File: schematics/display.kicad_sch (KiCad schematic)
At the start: 56 parts, among them Q11 2N3906, Q9 2N3906, U14 74AC138, U15 74HC245, U16 74HC245, U17 74HC245, U18 74HC245, U19 74HC4511, U20 74HC4511, U25 RED, U26 RED, U27 RED, U28 RED, U29 RED, U30 RED, U31 RED, U32 RED, U33 RED

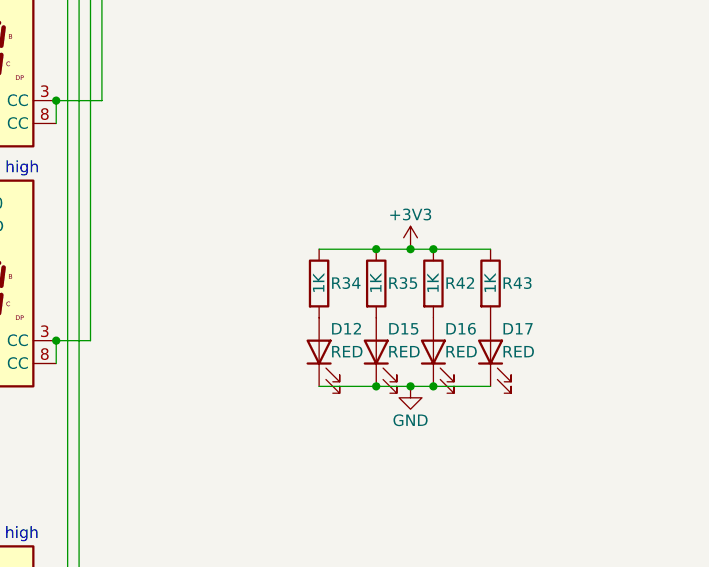
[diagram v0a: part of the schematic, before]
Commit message: increased resistor for colon LEDs
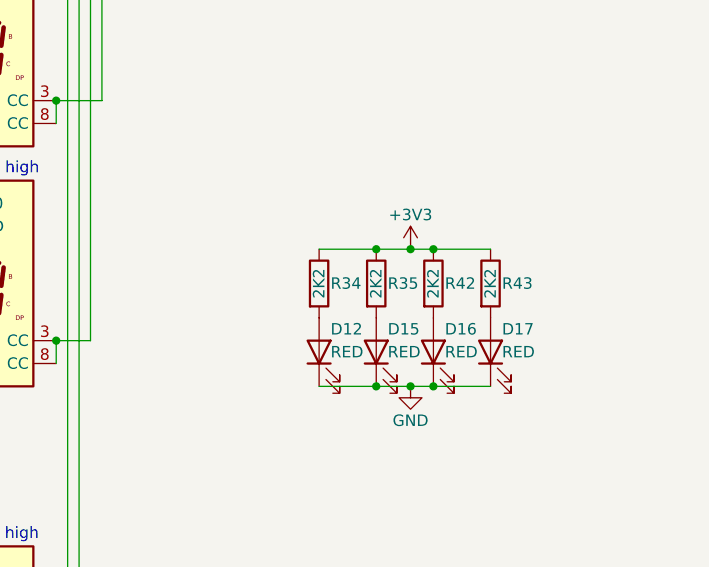
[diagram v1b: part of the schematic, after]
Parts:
- R34, R35, R42, R43: value 1K -> 2K2
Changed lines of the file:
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@@
 			)
 		)
-		(property "Value" "1K"
+		(property "Value" "2K2"
 			(at 238.76 92.71 90)
 			(show_name no)
@@
 			)
 		)
-		(property "Value" "1K"
+		(property "Value" "2K2"
 			(at 245.11 92.71 90)
 			(show_name no)
@@
 			)
 		)
-		(property "Value" "1K"
+		(property "Value" "2K2"
 			(at 226.06 92.71 90)
 			(show_name no)
@@
 			)
 		)
-		(property "Value" "1K"
+		(property "Value" "2K2"
 			(at 232.41 92.71 90)
 			(show_name no)

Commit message: started a second version
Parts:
- removed C32: 100N, Package_SO:SOIC-8_3.9x4.9mm_P1.27mm, symbol Device:C
- removed Q11, Q9: 2N3906, Package_TO_SOT_THT:TO-92_Inline, symbol Transistor_BJT:2N3906
- removed R17, R18: 4K7, symbol Device:R
- removed R19, R20, R21, R22, R23, R24, R25, R26, R27, R28, R29, R30, R31, R32, R33: 220R, symbol Device:R
- removed R57: 1K, symbol Device:R
- removed R58: 10K, symbol Device:R
- removed U15, U16, U17, U18: 74HC245, Package_SO:SOIC-16W_7.5x10.3mm_P1.27mm, symbol 74xx:74HC245
- removed U20: 74HC4511, symbol bvclock:74HC4511
- removed U25, U26, U27, U28, U29, U30, U31, U32, U33: RED, Display_7Segment:HDSP-A151, symbol Display_Character:HDSP-A153
- added Q1, Q2, Q21, Q22, Q3, Q4, Q5, Q6, Q7: 2N3904, Package_TO_SOT_THT:TO-92_Inline, symbol Transistor_BJT:2N3904
- added Q10, Q11, Q12, Q13, Q14, Q15, Q8, Q9: S9012, Package_TO_SOT_THT:TO-92_Inline, symbol Transistor_BJT:Q_PNP_EBC
- added R36, R38, R39, R40, R41, R46, R47: 10K, symbol Device:R
- added R48, R49, R51, R53, R54: 1K, symbol Device:R
- added R79: 75K, symbol Device:R
- added R81: 15K, symbol Device:R
- added U15, U21, U22, U23, U24, U25, U26, U3, U37: 5161BS, Display_7Segment:KCSC02-105, symbol Display_Character:KCSA02-105
- added U16, U17, U18, U20: 74HC251, Package_DIP:DIP-28_W15.24mm, symbol 74xx:74LS251
- R34, R35, R42, R43: value 2K2 -> 1K
- R52: value 10K -> 1K
- R55: value 680R -> 1K
- R56: value 150R -> 120R
- U14: value 74AC138 -> 74HC138
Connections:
- net ~{AMPM} is gone; now on an unnamed net: R50.2
- net +3V3: now also Q10.1 (E), Q11.1 (E), Q12.1 (E), Q13.1 (E), Q14.1 (E), Q15.1 (E), Q8.1 (E), Q9.1 (E), U16.16 (V_{CC}), U17.16 (V_{CC}), U18.16 (V_{CC}), U20.16 (V_{CC}), U37.3 (CA), U37.8 (CA); no longer R55.2, R56.2, U19.4 (~{BL}), U19.5 (~{LE})
- net CS0: now also U20.4 (I_{0})
- net CS1: now also U18.4 (I_{0})
- net CS2: now also U17.4 (I_{0})
- net CS3: now also U16.4 (I_{0})
- net DS0: now also U20.3 (I_{1})
- net DS1: now also U18.3 (I_{1})
- net DS2: now also U17.3 (I_{1})
- net DS3: now also U16.3 (I_{1})
- net GND: now also R56.1, U19.5 (~{LE}), Q1.1 (E), Q2.1 (E), Q21.1 (E), Q22.1 (E), Q3.1 (E), Q4.1 (E), Q5.1 (E), Q6.1 (E), Q7.1 (E), U16.1 (I_{3}), U16.12 (I_{7}), U16.14 (I_{5}), U16.7 (~{OE}), U16.8 (GND), U17.12 (I_{7}), U17.7 (~{OE}), U17.8 (GND), U18.7 (~{OE}), U18.8 (GND), U20.7 (~{OE}), U20.8 (GND); no longer U14.3 (A2)
- net HH0: now also U20.12 (I_{7})
- net HH1: now also U18.12 (I_{7})
- net HL0: now also U20.13 (I_{6})
- net HL1: now also U18.13 (I_{6})
- net HL2: now also U17.13 (I_{6})
- net HL3: now also U16.13 (I_{6})
- net MH0: now also U20.14 (I_{5})
- net MH1: now also U18.14 (I_{5})
- net MH2: now also U17.14 (I_{5})
- net ML0: now also U20.15 (I_{4})
- net ML1: now also U18.15 (I_{4})
- net ML2: now also U17.15 (I_{4})
- net ML3: now also U16.15 (I_{4})
- net SH0: now also U20.1 (I_{3})
- net SH1: now also U18.1 (I_{3})
- net SH2: now also U17.1 (I_{3})
- net SL0: now also U20.2 (I_{2})
- net SL1: now also U18.2 (I_{2})
- net SL2: now also U17.2 (I_{2})
- net SL3: now also U16.2 (I_{2})
- net ~{BL}: now also U19.4 (~{BL})
- net at U19.12 (b): now also R46.1
- net at R52.2: now also U14.12 (~{Y3})
- net at U19.10 (d): now also R40.1
- net at U19.6 (D_{3}): now also U16.5 (Y)
- net at U19.2 (D_{2}): now also U17.5 (Y)
- net at U19.1 (D_{1}): now also U18.5 (Y)
- net at U19.7 (D_{0}): now also U20.5 (Y)
- net at U19.13 (a): now also R47.1
- net at U19.11 (c): now also R41.1
- net at U14.14 (~{Y1}): now also R54.2
- net at U19.15 (f): now also R38.1
- net at U14.15 (~{Y0}): now also R55.2
- net at R50.1: now also Q10.2 (B)
- net at R55.1: now also Q15.2 (B)
- net at U19.9 (e): now also R39.1
- net at U14.13 (~{Y2}): now also R53.2
- net at U19.14 (g): now also R36.1
- net at U14.11 (~{Y4}): now also R51.2
- net at U14.7 (~{Y7}): now also R48.2
- net at U14.9 (~{Y6}): now also R49.2
- net S0 renamed SEL0
- net SEL0: now also U16.11 (S0), U17.11 (S0), U18.11 (S0), U20.11 (S0)
- net S1 renamed SEL1
- net SEL1: now also U16.10 (S1), U17.10 (S1), U18.10 (S1), U20.10 (S1)
- net ~{AM}: no longer names the net of R52.1
- net ~{AM}: now also Q12.2 (B)
- new net: Q22.2 (B), R81.2
- new net: Q22.3 (C), U37.1 (E), U37.10 (G), U37.5 (DP), U37.6 (B), U37.7 (A), U37.9 (F)
- new net: Q6.2 (B), R46.2
- new net: Q6.3 (C), U15.6 (B), U21.6 (B), U22.6 (B), U23.6 (B), U24.6 (B), U25.6 (B), U26.6 (B), U3.6 (B)
- new net: Q3.3 (C), U15.1 (E), U21.1 (E), U22.1 (E), U23.1 (E), U24.1 (E), U25.1 (E), U26.1 (E), U3.1 (E)
- new net: Q1.3 (C), U15.10 (G), U21.10 (G), U22.10 (G), U23.10 (G), U24.10 (G), U25.10 (G), U26.10 (G), U3.10 (G)
- new net: Q4.3 (C), U15.2 (D), U21.2 (D), U22.2 (D), U23.2 (D), U24.2 (D), U25.2 (D), U26.2 (D), U3.2 (D)
- new net: Q13.3 (C), U24.3 (CA), U24.8 (CA)
- new net: Q5.3 (C), U15.4 (C), U21.4 (C), U22.4 (C), U23.4 (C), U24.4 (C), U25.4 (C), U26.4 (C), U3.4 (C)
- new net: R56.2, U24.5 (DP)
- new net: Q7.3 (C), U15.7 (A), U21.7 (A), U22.7 (A), U23.7 (A), U24.7 (A), U25.7 (A), U26.7 (A), U3.7 (A)
- new net: Q2.3 (C), U15.9 (F), U21.9 (F), U22.9 (F), U23.9 (F), U24.9 (F), U25.9 (F), U26.9 (F), U3.9 (F)
- new net: Q15.3 (C), U26.3 (CA), U26.8 (CA)
- new net: Q4.2 (B), R40.2
- new net: Q3.2 (B), R39.2
- new net: Q7.2 (B), R47.2
- new net: Q1.2 (B), R36.2
- new net: Q8.2 (B), R48.1
- new net: Q11.3 (C), U22.3 (CA), U22.8 (CA)
- new net: Q12.3 (C), U23.3 (CA), U23.8 (CA)
- new net: Q2.2 (B), R38.2
- new net: Q11.2 (B), R51.1
- new net: Q21.2 (B), R79.2
- new net: Q10.3 (C), U21.3 (CA), U21.8 (CA)
- new net: Q13.2 (B), R53.1
- new net: Q14.2 (B), R54.1
- new net: Q14.3 (C), U25.3 (CA), U25.8 (CA)
- new net: Q9.2 (B), R49.1
- new net: Q9.3 (C), U15.3 (CA), U15.8 (CA)
- new net: Q5.2 (B), R41.2
- new net: Q21.3 (C), U37.4 (C)
- new net AM: R79.1
- new net AMPM: R81.1
- new net SEL2: U14.3 (C), U16.9 (S2), U17.9 (S2), U18.9 (S2), U20.9 (S2)
- new net ~{HHSEL}: Q8.3 (C), U3.3 (CA), U3.8 (CA)
- no-connect marks 14 -> 12
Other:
- note removed: "AM/PM"
- note removed: "centiseconds"
- note removed: "deciseconds"
- note removed: "hours high"
- note removed: "hours low"
- note removed: "minutes high"
- note removed: "minutes low"
- note removed: "seconds high"
- note removed: "seconds low"
- moved on the sheet: C26, C27, C28, C29, C30, C31, D12, D15, D16, D17, R34, R35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

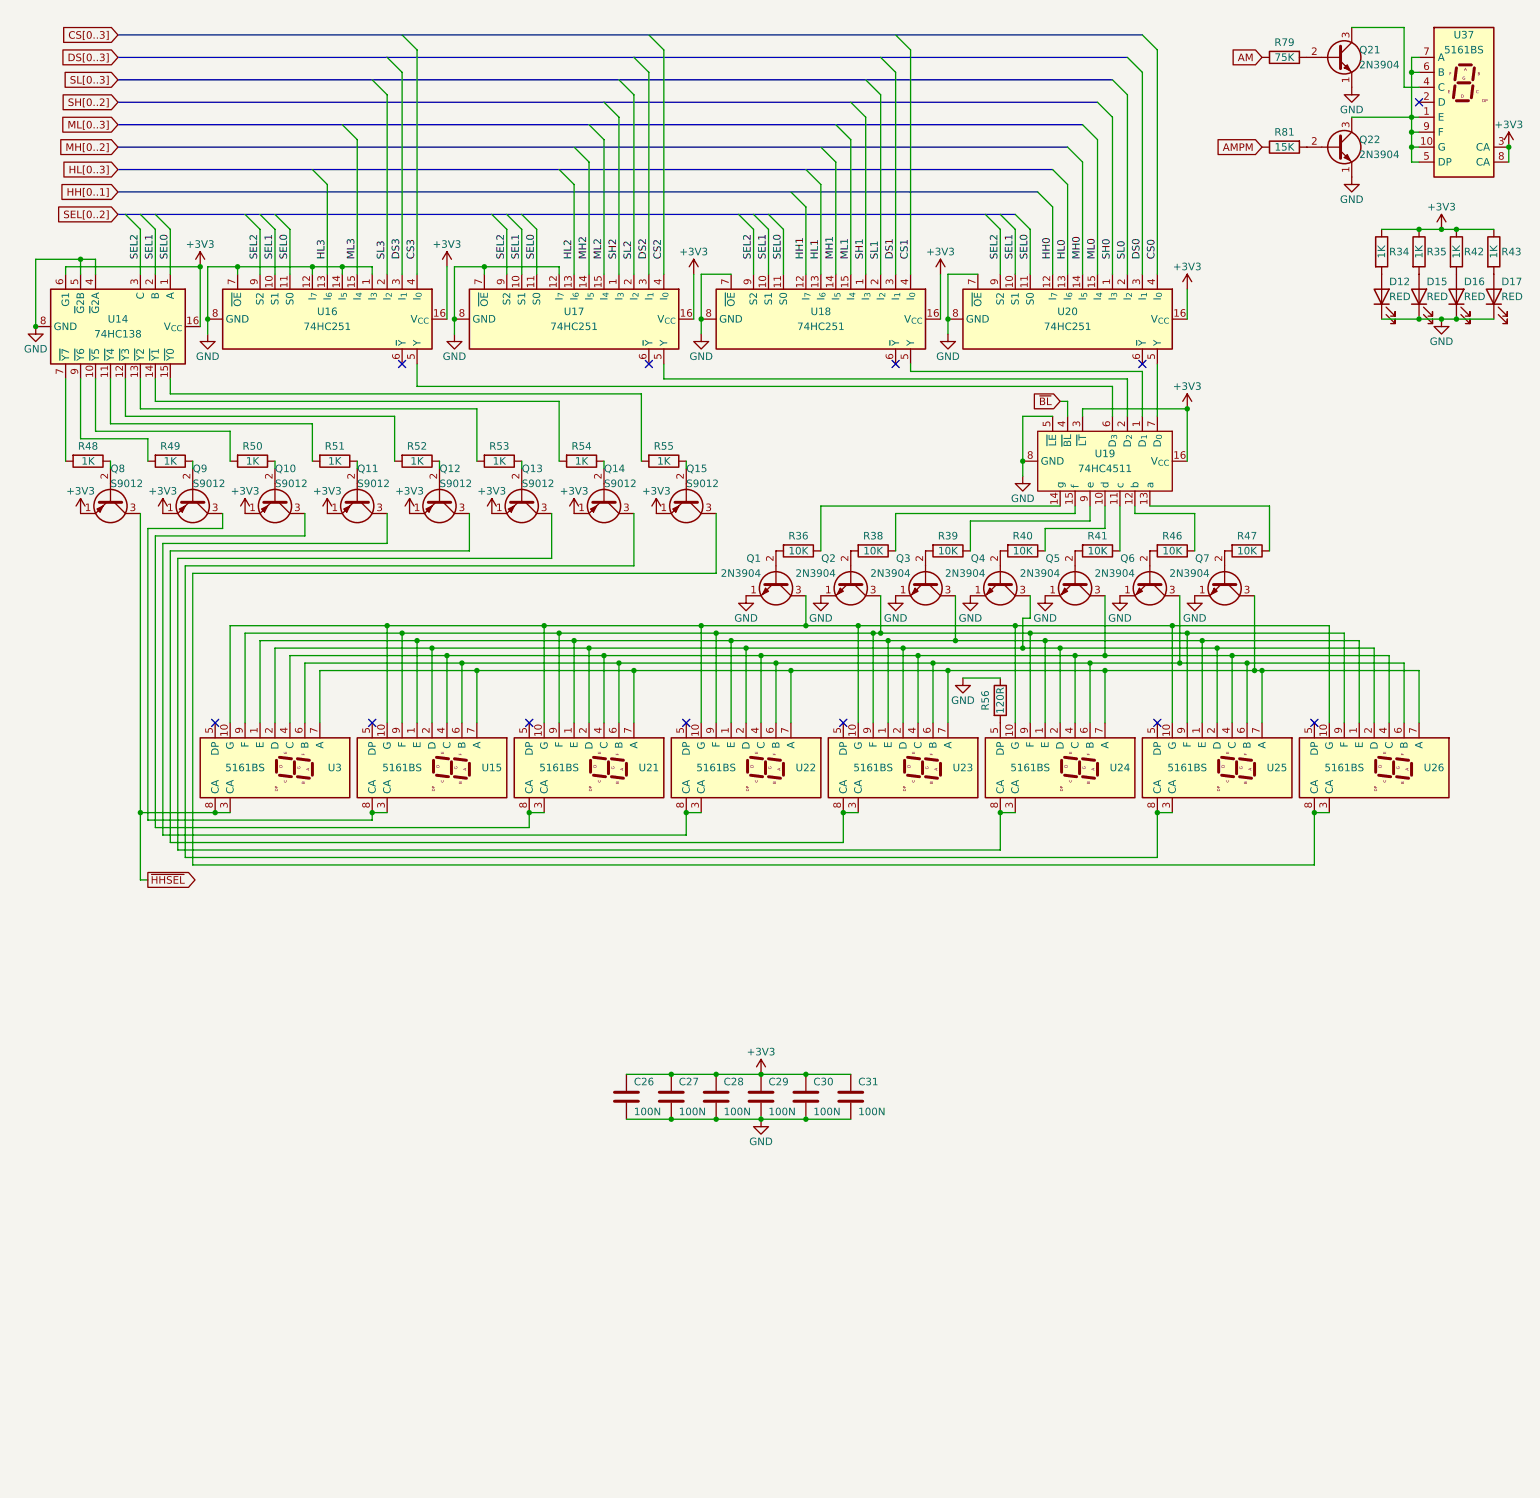
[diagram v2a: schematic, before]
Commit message: switched to diode logic; added LED dimmer
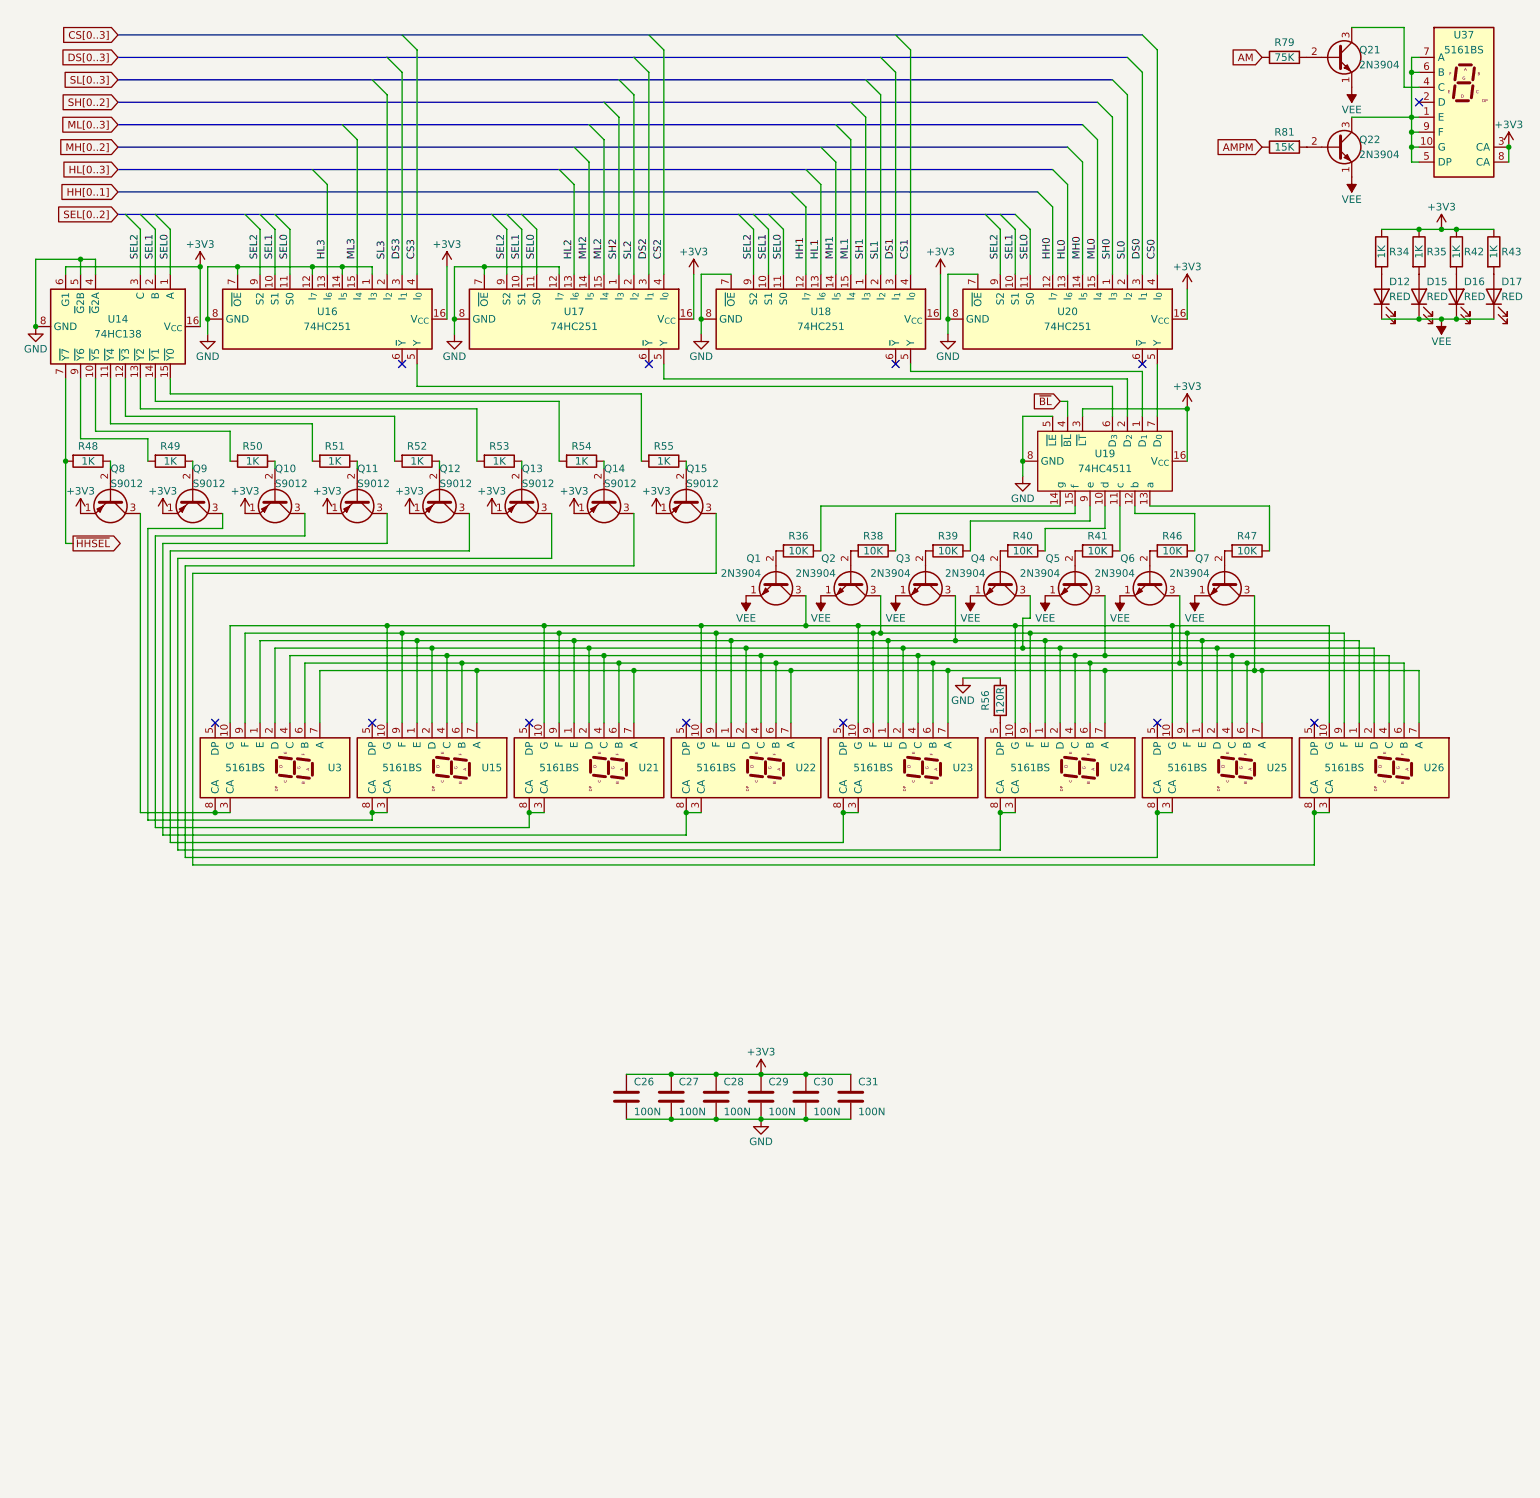
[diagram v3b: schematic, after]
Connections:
- net GND: no longer D12.1 (K), D15.1 (K), D16.1 (K), D17.1 (K), Q1.1 (E), Q2.1 (E), Q21.1 (E), Q22.1 (E), Q3.1 (E), Q4.1 (E), Q5.1 (E), Q6.1 (E), Q7.1 (E)
- net ~{HHSEL}: now also R48.2, U14.7 (~{Y7}); no longer Q8.3 (C), U3.3 (CA), U3.8 (CA)
- new net: Q8.3 (C), U3.3 (CA), U3.8 (CA)
- new net VEE: D12.1 (K), D15.1 (K), D16.1 (K), D17.1 (K), Q1.1 (E), Q2.1 (E), Q21.1 (E), Q22.1 (E), Q3.1 (E), Q4.1 (E), Q5.1 (E), Q6.1 (E), Q7.1 (E)

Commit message: re-annotate
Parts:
- renumbered C26 to C20, C27 to C21, C28 to C22, C29 to C23, C30 to C24, C31 to C25, D12 to D24, D15 to D25, D16 to D26, D17 to D27, Q8 to Q1, Q2 to Q10, Q3 to Q11, Q4 to Q12, Q5 to Q13, Q6 to Q14, Q7 to Q15, Q21 to Q16, Q22 to Q17, Q9 to Q2, Q10 to Q3, Q11 to Q4, Q12 to Q5, Q13 to Q6, Q14 to Q7, Q15 to Q8, Q1 to Q9, R48 to R22, R49 to R23, R50 to R24, R51 to R25, R52 to R26, R53 to R27, R54 to R28, R55 to R29, R36 to R30, R38 to R31, R39 to R32, R56 to R33, R40 to R34, R41 to R35, R46 to R36, R47 to R37, R79 to R38, R81 to R39, R34 to R40, R35 to R41, U14 to U12, U3 to U13, U16 to U14, U17 to U16, U21 to U17, U22 to U18, U18 to U19, U23 to U20, U24 to U21, U20 to U22, U19 to U23, U25 to U24, U26 to U25, U37 to U26

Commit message: diode matrix rom
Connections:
- net ~{BL} is gone; now on net GND: U23.4 (~{BL})
- net GND: no longer U14.12 (I_{7}), U16.12 (I_{7})
- net AMPM renamed TW
- new net HH2: U16.12 (I_{7})
- new net HH3: U14.12 (I_{7})
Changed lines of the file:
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@@
 	)
 	(junction
+		(at 186.69 78.74)
+		(diameter 0)
+		(color 0 0 0 0)
+	)
+	(junction
 		(at 144.78 190.5)
 		(diameter 0)
@@
 	)
 	(junction
-		(at 60.96 53.34)
-		(diameter 0)
-		(color 0 0 0 0)
-	)
-	(junction
 		(at 212.09 116.84)
 		(diameter 0)
@@
 	)
 	(junction
-		(at 90.17 53.34)
-		(diameter 0)
-		(color 0 0 0 0)
-	)
-	(junction
 		(at 129.54 198.12)
 		(diameter 0)
@@
 	)
 	(bus_entry
+		(at 100.33 40.64)
+		(size 2.54 2.54)
+		(stroke
+			(width 0)
+			(type default)
+		)
+	)
+	(bus_entry
 		(at 142.24 40.64)
 		(size 2.54 2.54)
@@
 	)
 	(bus_entry
+		(at 58.42 40.64)
+		(size 2.54 2.54)
+		(stroke
+			(width 0)
+			(type default)
+		)
+	)
+	(bus_entry
 		(at 201.93 13.97)
 		(size 2.54 2.54)
@@
 	(wire
 		(pts
+			(xy 60.96 43.18) (xy 60.96 54.61)
+		)
+		(stroke
+			(width 0)
+			(type default)
+		)
+	)
+	(wire
+		(pts
 			(xy 96.52 46.99) (xy 96.52 54.61)
 		)
@@
 	(wire
 		(pts
+			(xy 186.69 78.74) (xy 189.23 78.74)
+		)
+		(stroke
+			(width 0)
+			(type default)
+		)
+	)
+	(wire
+		(pts
 			(xy 204.47 16.51) (xy 204.47 54.61)
 		)
@@
 	(wire
 		(pts
-			(xy 102.87 53.34) (xy 102.87 54.61)
+			(xy 102.87 43.18) (xy 102.87 54.61)
 		)
 		(stroke
@@
 	(wire
 		(pts
-			(xy 102.87 53.34) (xy 90.17 53.34)
-		)
-		(stroke
-			(width 0)
-			(type default)
-		)
-	)
-	(wire
-		(pts
 			(xy 85.09 64.77) (xy 85.09 62.23)
 		)
@@
 	(wire
 		(pts
-			(xy 85.09 53.34) (xy 85.09 62.23)
-		)
-		(stroke
-			(width 0)
-			(type default)
-		)
-	)
-	(wire
-		(pts
-			(xy 66.04 53.34) (xy 60.96 53.34)
+			(xy 85.09 54.61) (xy 85.09 62.23)
 		)
 		(stroke
@@
 	(wire
 		(pts
-			(xy 60.96 53.34) (xy 48.26 53.34)
+			(xy 48.26 53.34) (xy 66.04 53.34)
 		)
 		(stroke
@@
 	(wire
 		(pts
-			(xy 60.96 53.34) (xy 60.96 54.61)
-		)
-		(stroke
-			(width 0)
-			(type default)
-		)
-	)
-	(wire
-		(pts
 			(xy 81.28 118.11) (xy 54.61 118.11)
 		)
@@
 	(wire
 		(pts
-			(xy 187.96 76.2) (xy 189.23 76.2)
-		)
-		(stroke
-			(width 0)
-			(type default)
-		)
-	)
-	(wire
-		(pts
 			(xy 132.08 116.84) (xy 132.08 130.81)
 		)
@@
 	(wire
 		(pts
-			(xy 90.17 53.34) (xy 90.17 54.61)
-		)
-		(stroke
-			(width 0)
-			(type default)
-		)
-	)
-	(wire
-		(pts
 			(xy 121.92 198.12) (xy 129.54 198.12)
 		)
@@
 	(wire
 		(pts
-			(xy 90.17 53.34) (xy 85.09 53.34)
+			(xy 90.17 54.61) (xy 85.09 54.61)
 		)
 		(stroke
@@
 	(wire
 		(pts
-			(xy 189.23 76.2) (xy 189.23 78.74)
-		)
-		(stroke
-			(width 0)
-			(type default)
-		)
-	)
-	(wire
-		(pts
 			(xy 40.64 105.41) (xy 40.64 154.94)
 		)
@@
 		)
 	)
+	(label "HH2"
+		(at 102.87 52.07 90)
+		(effects
+			(font
+				(size 1.27 1.27)
+			)
+			(justify left bottom)
+		)
+	)
 	(label "MH2"
 		(at 107.95 52.07 90)
@@
 		)
 	)
+	(label "HH3"
+		(at 60.96 52.07 90)
+		(effects
+			(font
+				(size 1.27 1.27)
+			)
+			(justify left bottom)
+		)
+	)
 	(label "SEL1"
 		(at 96.52 52.07 90)
@@
 		)
 	)
-	(global_label "AMPM"
+	(global_label "TW"
 		(shape input)
 		(at 222.25 33.02 180)
@@
 		)
 		(property "Intersheetrefs" "${INTERSHEET_REFS}"
-			(at 214.0034 33.02 0)
+			(at 216.8458 33.02 0)
 			(hide yes)
 			(show_name no)
@@
 		)
 	)
-	(global_label "~{BL}"
-		(shape input)
-		(at 187.96 76.2 180)
-		(fields_autoplaced yes)
-		(effects
-			(font
-				(size 1.27 1.27)
-			)
-			(justify right)
-		)
-		(property "Intersheetrefs" "${INTERSHEET_REFS}"
-			(at 182.6767 76.2 0)
-			(hide yes)
-			(show_name no)
-			(do_not_autoplace no)
-			(effects
-				(font
-					(size 1.27 1.27)
-				)
-				(justify right)
-			)
-		)
-	)
 	(global_label "SH[0..2]"
 		(shape input)
@@
 		)
 	)
-	(global_label "HH[0..1]"
+	(global_label "HH[0..3]"
 		(shape input)
 		(at 27.94 40.64 180)
